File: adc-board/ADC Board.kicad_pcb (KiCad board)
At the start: 4 copper layers, 92.7 x 83.8 mm, 118 parts, among them J1 BHR-44-HUA, J2 ST-LINK/V2, J3 USART1, J4 USART6, J5 UE27AC5410H, J6 54601-908WPLF, J7 AltPowerInput, J8 USBPowerJumper, U0 STM32H743ZITx, U1 Opamp_Quad_Generic, U10 MCP1501-20E/SN, U13 3.3V Reg, U14 ISL83490, U2 Opamp_Quad_Generic, U29 AP7361C-33E-13, U3 Opamp_Quad_Generic, U4 Opamp_Quad_Generic, U5 Opamp_Quad_Generic, U6 Opamp_Quad_Generic, U9 USBLC6-2SC6, Y1 NX3225GD-8.000M-EXS00A-CG04874

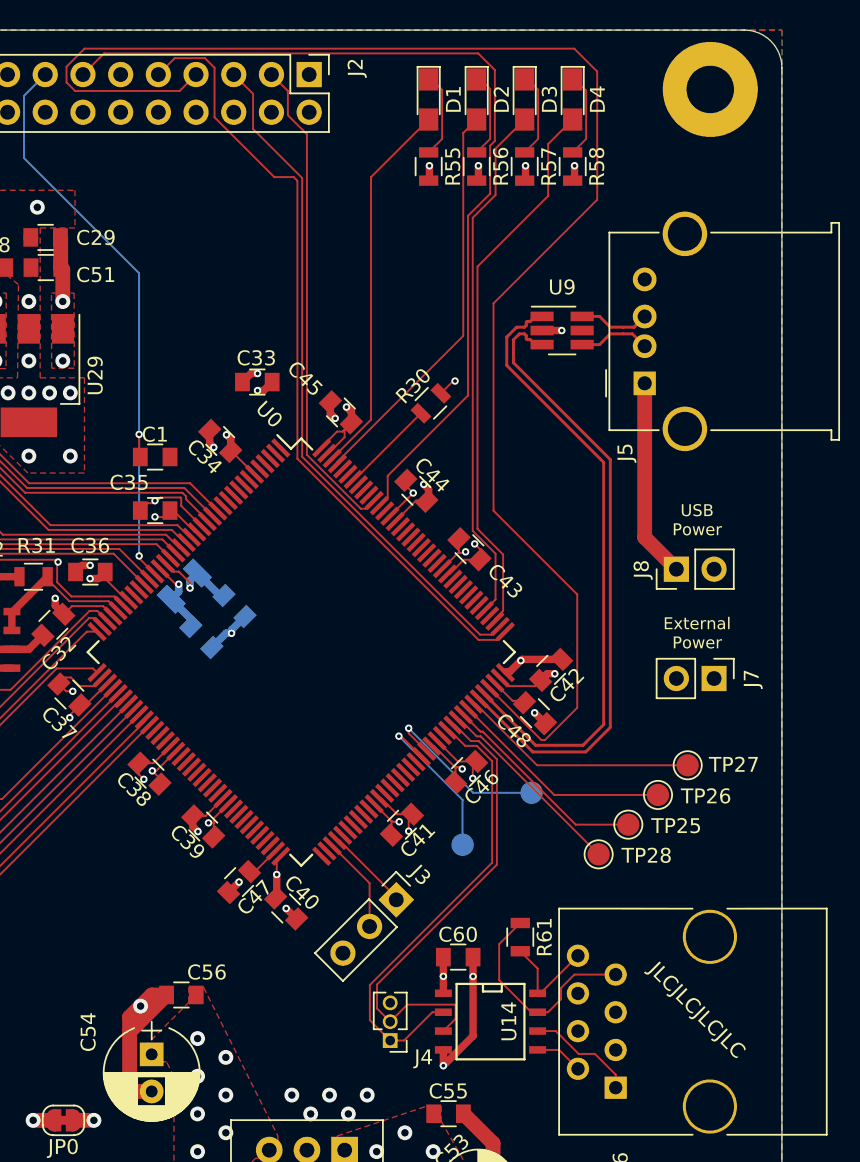
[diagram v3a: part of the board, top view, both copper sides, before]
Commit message: USB VBUS sensing; rearrange/correct USARTs
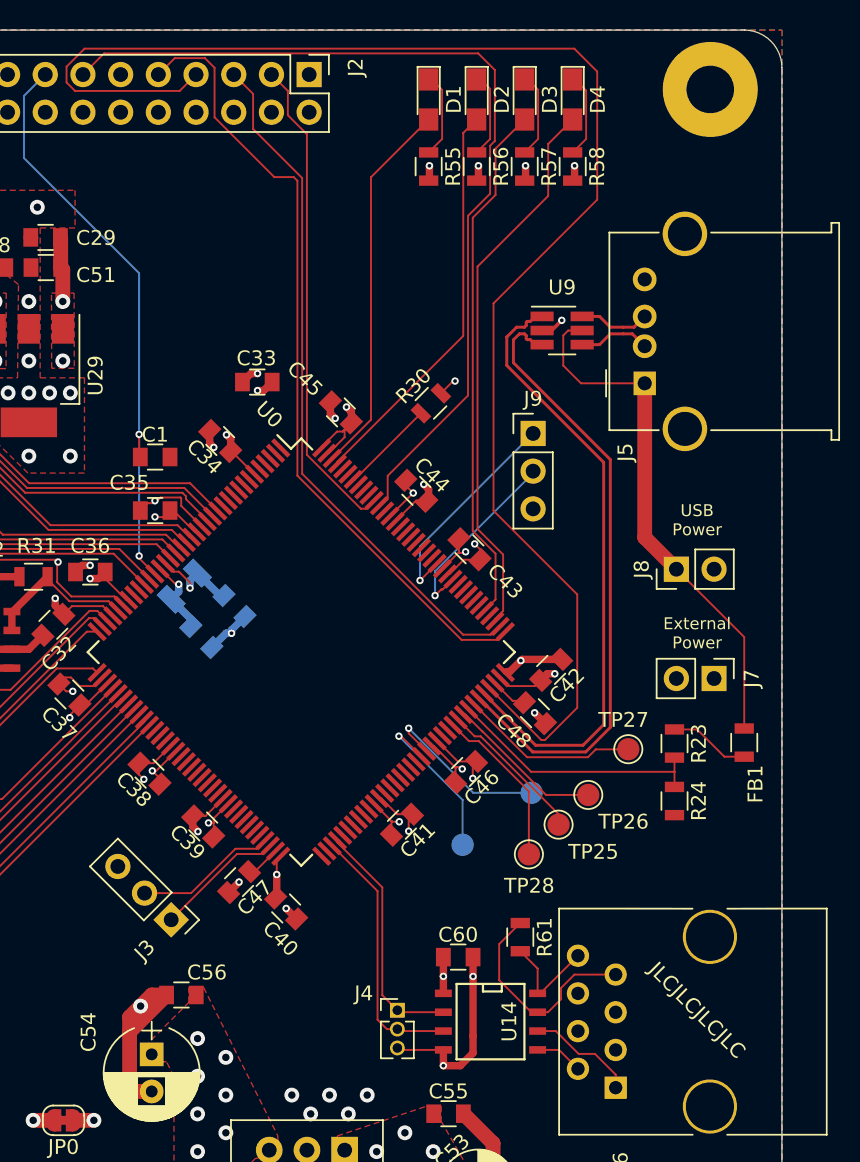
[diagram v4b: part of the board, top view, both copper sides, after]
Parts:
- added FB1: Ferrite_Bead_Small, Inductors_SMD:L_0805, F.Cu at (121.9, 95.0)
- added J9: USART2, Pin_Headers:Pin_Header_Straight_1x03_Pitch2.54mm, F.Cu at (107.7, 74.2)
- added R23: 2200, Resistors_SMD:R_0805, F.Cu at (117.2, 95.1)
- added R24: 4300, Resistors_SMD:R_0805, F.Cu at (117.2, 98.9)
- J3: value USART1 -> USART3
- J4: value USART6 -> USART1
- moved J3 15.2 mm to (83.3, 106.9), turned to 225 degrees
- moved TP25 4.70 mm to (109.4, 100.5)
- moved TP26 4.70 mm to (111.4, 98.5)
- moved TP28 4.70 mm to (107.4, 102.5)
- moved TP27 4.15 mm to (114.1, 95.4)
- moved J4 2.10 mm to (98.6, 113.0), turned to 0 degrees
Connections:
- J3 pad 1: /USART1_RX -> /USART3_RX
- J3 pad 2: /USART1_TX -> /USART3_TX
- J4 pad 1: /USART6_RX -> /USART1_RX
- J4 pad 2: /USART6_TX -> /USART1_TX
- J5 pad 1: Net-(J5-Pad1) -> /USB_VBUS
- J8 pad 1: Net-(J5-Pad1) -> /USB_VBUS
- U0 pad 100: Net-(TP25-Pad1) -> Net-(TP26-Pad1)
- U0 pad 101: Net-(TP26-Pad1) -> /VBUS_SENSE
- U0 pad 119: (no net) -> /USART2_TX
- U0 pad 122: (no net) -> /USART2_RX
- U0 pad 69: (no net) -> /USART3_TX
- U0 pad 70: (no net) -> /USART3_RX
- U0 pad 97: /USART6_RX -> (no net)
- U0 pad 98: /USART6_TX -> Net-(TP28-Pad1)
- U0 pad 99: Net-(TP28-Pad1) -> Net-(TP25-Pad1)
- U14 pad 2: /USART6_RX -> /USART1_RX
- U14 pad 3: /USART6_TX -> /USART1_TX
- U9 pad 5: (no net) -> /USB_VBUS
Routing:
- net /USB_VBUS: track 0.00 -> 35.5 mm
- net /USART6_TX: track 32.3 -> 0.00 mm
- net /USART6_RX: track 31.0 -> 0.00 mm
- net /VBUS_SENSE: track 0.00 -> 17.6 mm
- net /USART2_RX: track 0.00 -> 14.7 mm, vias 0 -> 1
- net Net-(J5-Pad1): track 13.4 -> 0.00 mm
- net /USART2_TX: track 0.00 -> 12.8 mm, vias 0 -> 1
- net /USART1_TX: track 6.48 -> 17.7 mm
- net /USART1_RX: track 5.71 -> 16.4 mm
- net /USART3_TX: track 0.00 -> 9.59 mm
- net /USART3_RX: track 0.00 -> 8.74 mm
- net /VBUS_FB: track 0.00 -> 5.46 mm
- net Net-(TP26-Pad1): track 15.1 -> 10.7 mm
- net GNDD: track 84.6 -> 88.7 mm
- net Net-(TP25-Pad1): track 14.2 -> 10.1 mm
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
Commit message: move USB ferrite closer to connector; add VCC pad near BOOT pulldown
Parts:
- FB1: value Ferrite_Bead_Small -> MPZ2012S601AT000
- U29: value AP7361C-33E-13 -> AP2114HA-3.3TRG1
- moved FB1 26.5 mm to (111.0, 70.8), turned to 90 degrees
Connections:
- FB1 pad 2: /VBUS_FB -> Net-(FB1-Pad2)
- J5 pad 1: /USB_VBUS -> Net-(FB1-Pad2)
- R23 pad 1: /VBUS_FB -> /USB_VBUS
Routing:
- net /VBUS_FB: track 5.46 -> 0.00 mm
- net Net-(FB1-Pad2): track 0.00 -> 4.54 mm
- net /USB_VBUS: track 35.5 -> 38.0 mm
- net +3V3: vias 23 -> 24

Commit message: Rev0 of boards; added text
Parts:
- moved JP0 51.3 mm to (80.5, 69.3)
- moved C51 4.26 mm to (71.1, 61.0), turned to 0 degrees
- moved C29 2.03 mm to (74.9, 63.0)
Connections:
- C51 pad 1: +5V -> +3.3VA
- U10 pad 1: +5V -> +3.3VA
- U10 pad 3: +5V -> +3.3VA
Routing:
- net GNDD: track 88.7 -> 75.6 mm, vias 39 -> 38
- net +3.3VA: track 85.8 -> 92.7 mm, vias 10 -> 11
- net +5V: track 7.66 -> 2.92 mm, vias 8 -> 6
- net GNDA: track 79.8 -> 79.4 mm, vias 37 -> 36
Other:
- board text added: "http://github.com/jkominek/piano-conversion ADC Board - Rev 0"

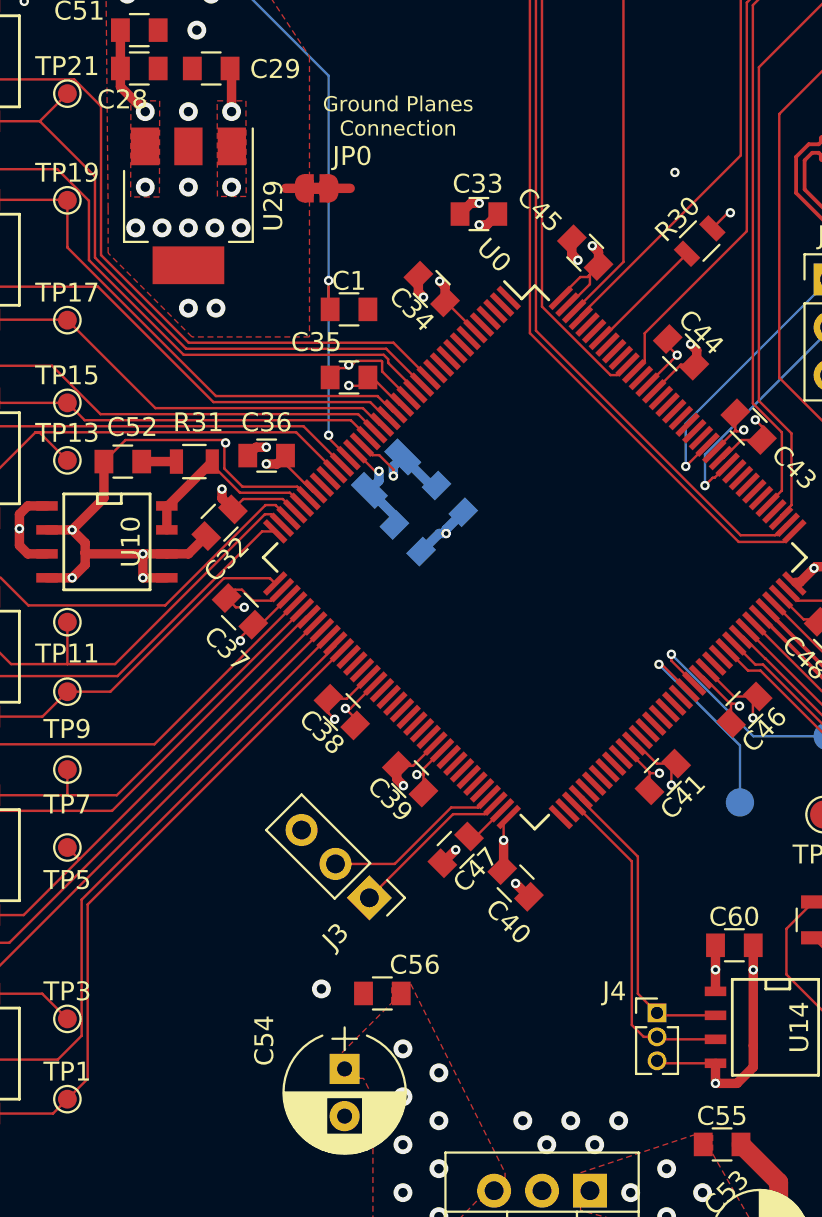
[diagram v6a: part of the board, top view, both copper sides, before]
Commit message: correct the jtag header
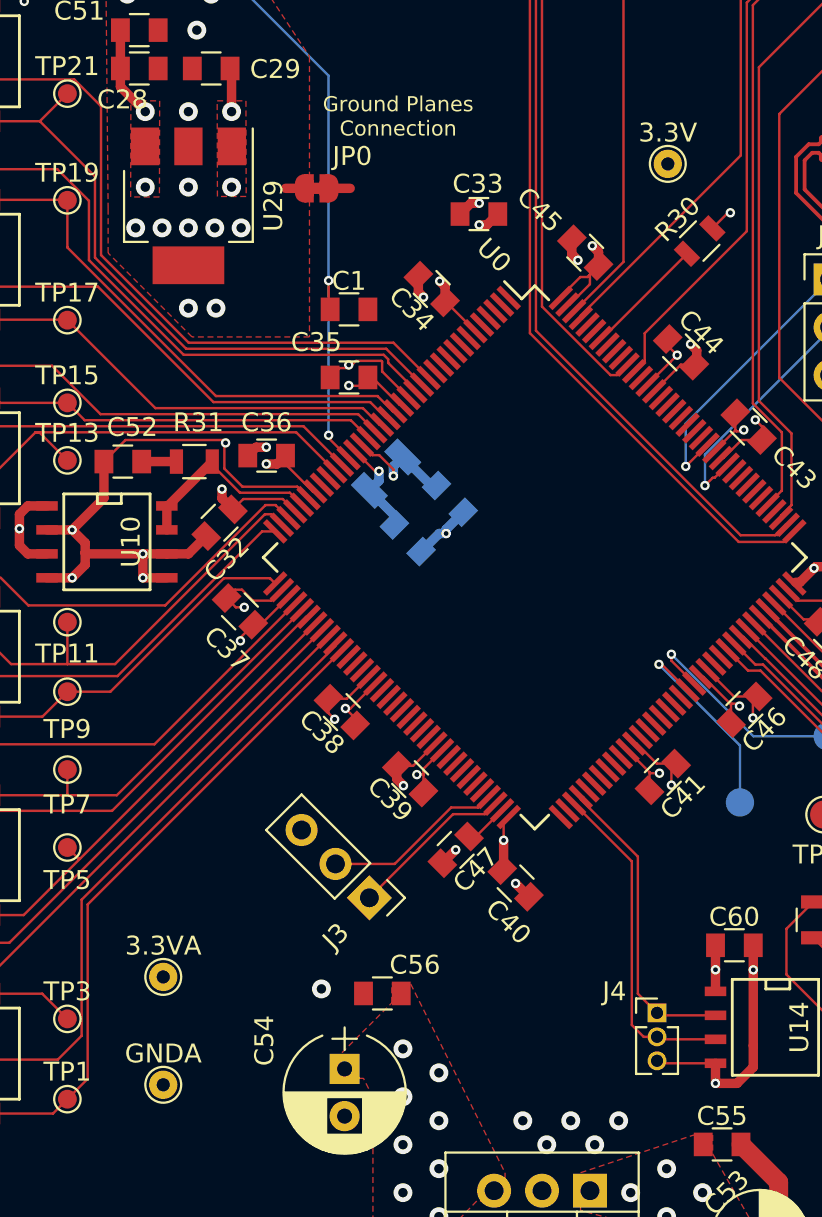
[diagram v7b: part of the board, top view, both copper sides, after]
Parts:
- added 3.3V: TestPoint_THTPad_D1.5mm_Drill0.7mm, Testpoint:TestPoint_THTPad_D1.5mm_Drill0.7mm, F.Cu at (99.1, 68.0)
- added 3.3VA: TestPoint_THTPad_D1.5mm_Drill0.7mm, Testpoint:TestPoint_THTPad_D1.5mm_Drill0.7mm, F.Cu at (72.4, 111.1)
- added GNDA: TestPoint_THTPad_D1.5mm_Drill0.7mm, Testpoint:TestPoint_THTPad_D1.5mm_Drill0.7mm, F.Cu at (72.4, 116.8)
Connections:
- J2 pad 1: (no net) -> +3V3
- J2 pad 2: (no net) -> +3V3
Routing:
- net +3V3: vias 24 -> 23

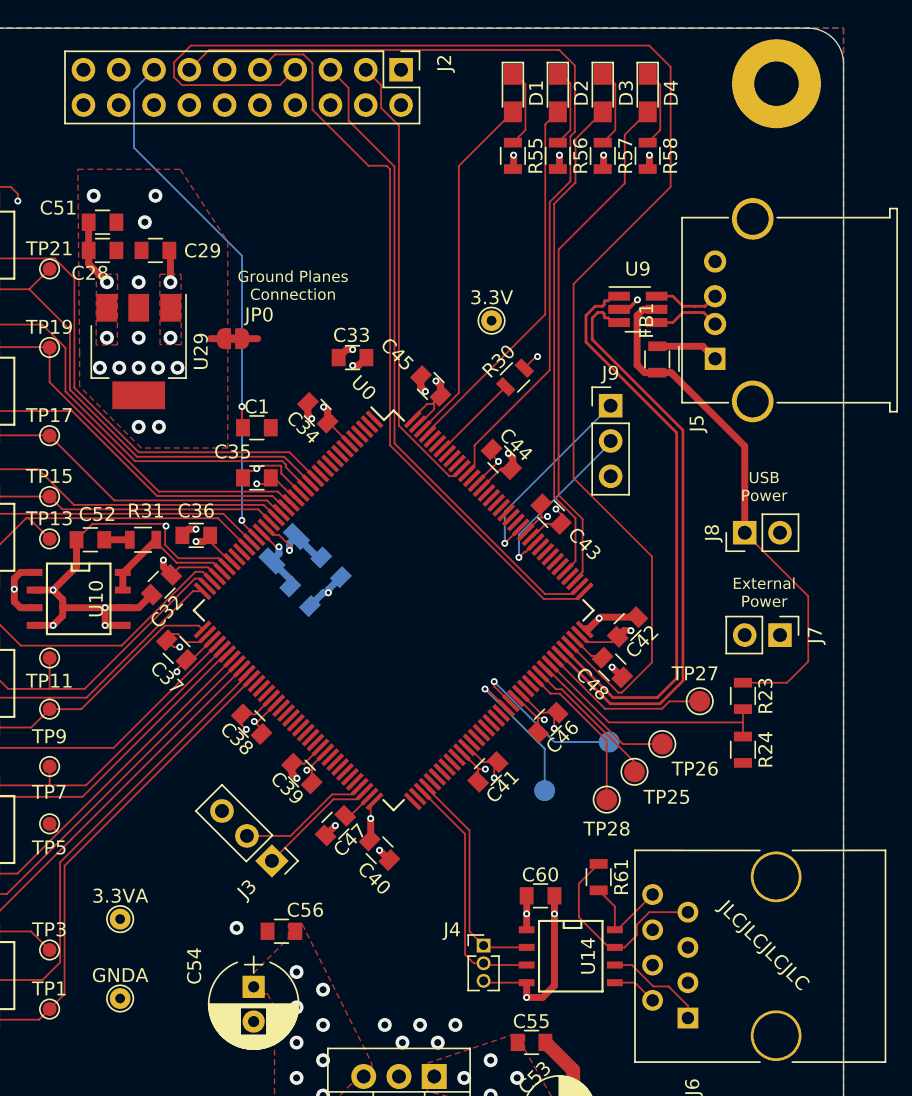
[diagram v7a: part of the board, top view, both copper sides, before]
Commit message: Various changes from initial stages of board bringup
* Add thermal relief to lots of connections
* +3.3V power LED
* BOOT0 jumper for pull to +3.3V
* Reorder USB TVS & ferrite bead
* Tweaking and compaction of some traces
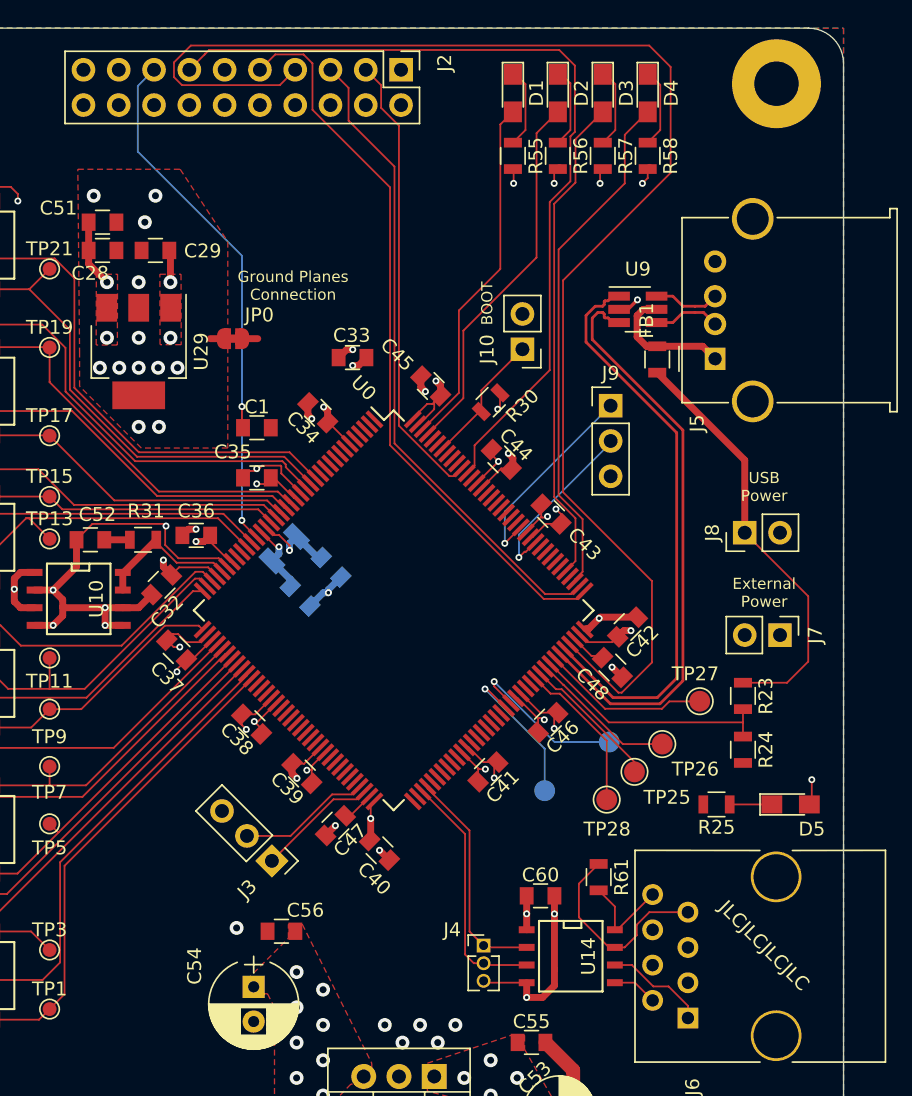
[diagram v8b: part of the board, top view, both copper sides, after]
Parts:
- removed 3.3V, 3.3VA, GNDA: TestPoint_THTPad_D1.5mm_Drill0.7mm, Testpoint:TestPoint_THTPad_D1.5mm_Drill0.7mm
- added D5: LED, LEDs:LED_0805_HandSoldering, F.Cu at (120.7, 102.9)
- added J10: BootJumper, Pin_Headers:Pin_Header_Straight_1x02_Pitch2.54mm, F.Cu at (101.3, 70.1)
- added R25: CL, Resistors_SMD:R_0805, F.Cu at (115.3, 102.9)
- moved R30 2.50 mm to (99.1, 73.9)
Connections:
- U9 pad 5: /USB_VBUS -> Net-(FB1-Pad2)
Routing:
- net /USB_VBUS: track 38.0 -> 30.6 mm
- net Net-(FB1-Pad2): track 4.54 -> 9.38 mm
- net /BOOT0: track 6.41 -> 9.63 mm
- net Net-(D5-Pad1): track 0.00 -> 3.03 mm
- net +3V3: track 52.4 -> 54.3 mm, vias 23 -> 24
- net GNDD: track 75.6 -> 76.4 mm
- net /JTCK: track 53.9 -> 53.1 mm
- net /JTMS: track 103.7 -> 104.3 mm
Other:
- board text added: "BOOT"
